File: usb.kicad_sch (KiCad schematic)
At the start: 9 parts, among them J4 CONN_02X03, U1 LFE5U-85F-6BG381C, U6 FT231XS, Y1 ECS-1612MV-250-CN-TR

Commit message: in progress, placement happend -- working on wiring
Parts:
- J4: footprint Socket_Strips:Socket_Strip_Straight_2x03 -> Connector_PinSocket_2.54mm:PinSocket_2x03_P2.54mm_Vertical

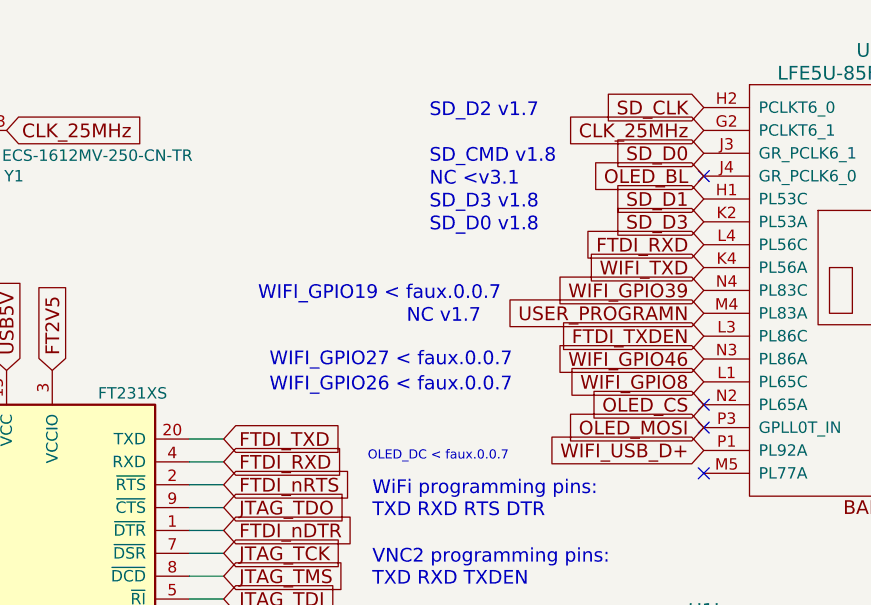
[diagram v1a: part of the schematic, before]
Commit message: done with routing
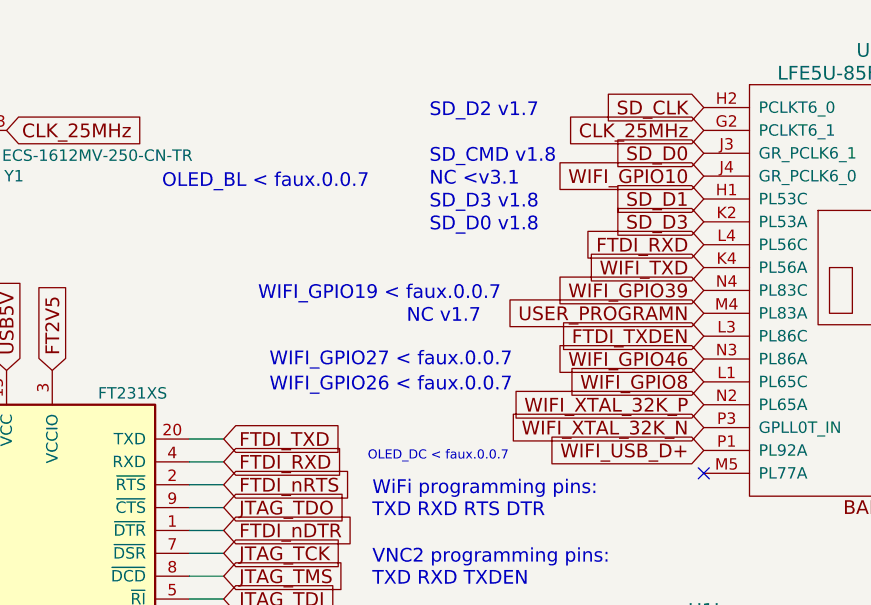
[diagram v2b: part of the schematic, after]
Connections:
- net OLED_BL renamed WIFI_GPIO10
- net OLED_CS renamed WIFI_XTAL_32K_P
- net OLED_MOSI renamed WIFI_XTAL_32K_N
- no-connect marks 8 -> 5
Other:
- note added: "OLED_BL < faux.0.0.7"
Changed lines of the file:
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@@
+		)
+	)
+	(text "OLED_BL < faux.0.0.7"
+		(exclude_from_sim no)
+		(at 159.512 43.434 0)
+		(effects
+			(font
+				(size 1.524 1.524)
+			)
+			(justify left bottom)
 		)
 	)
@@
 	)
 	(no_connect
-		(at 219.71 69.85)
-	)
-	(no_connect
-		(at 219.71 67.31)
-	)
-	(no_connect
 		(at 46.99 50.8)
 	)
@@
 		(at 219.71 74.93)
 	)
-	(no_connect
-		(at 219.71 41.91)
-	)
 	(wire
 		(pts
@@
 		)
 	)
-	(global_label "OLED_BL"
+	(global_label "WIFI_GPIO10"
 		(shape input)
 		(at 219.71 41.91 180)
@@
 		)
 	)
-	(global_label "OLED_MOSI"
+	(global_label "WIFI_XTAL_32K_N"
 		(shape input)
 		(at 219.71 69.85 180)
@@
 		)
 	)
-	(global_label "OLED_CS"
+	(global_label "WIFI_XTAL_32K_P"
 		(shape input)
 		(at 219.71 67.31 180)

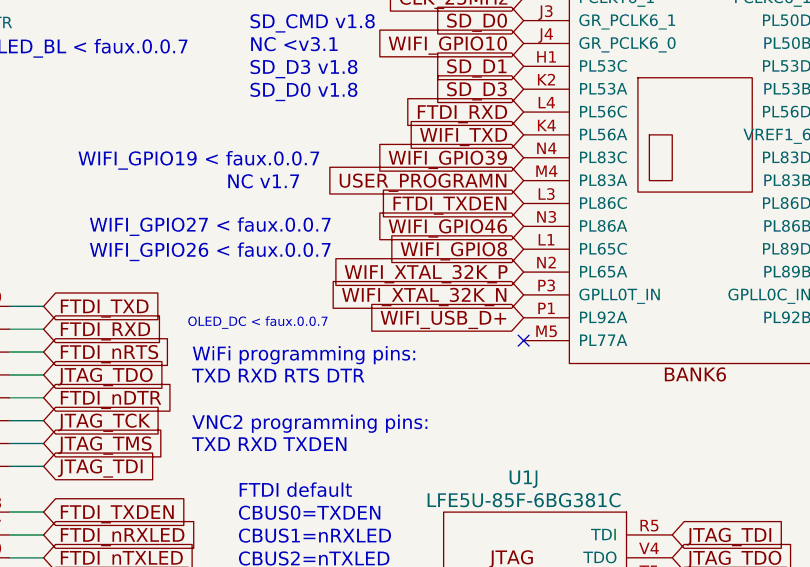
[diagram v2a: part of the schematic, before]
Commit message: fix diff pairs
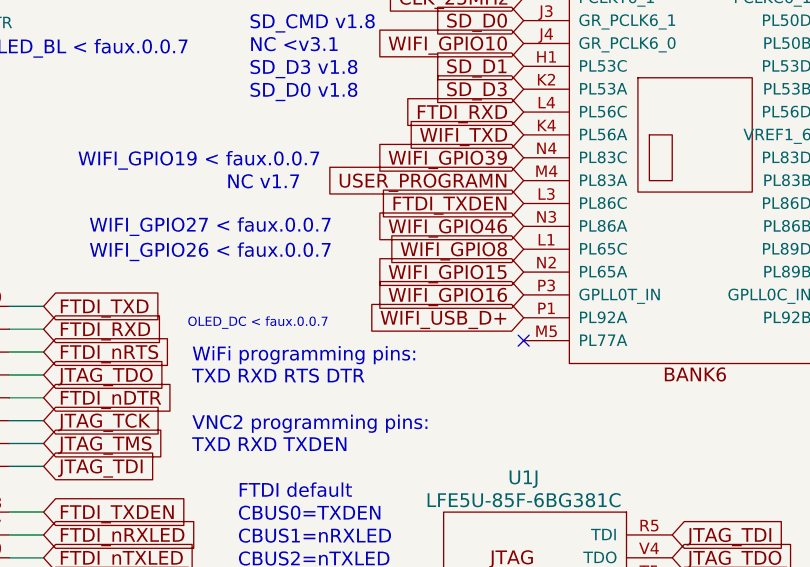
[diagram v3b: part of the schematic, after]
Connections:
- net WIFI_XTAL_32K_N renamed WIFI_GPIO16
- net WIFI_XTAL_32K_P renamed WIFI_GPIO15
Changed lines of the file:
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@@
 		)
 	)
-	(global_label "WIFI_XTAL_32K_N"
+	(global_label "WIFI_GPIO16"
 		(shape input)
 		(at 219.71 69.85 180)
@@
 		)
 	)
-	(global_label "WIFI_XTAL_32K_P"
+	(global_label "WIFI_GPIO15"
 		(shape input)
 		(at 219.71 67.31 180)

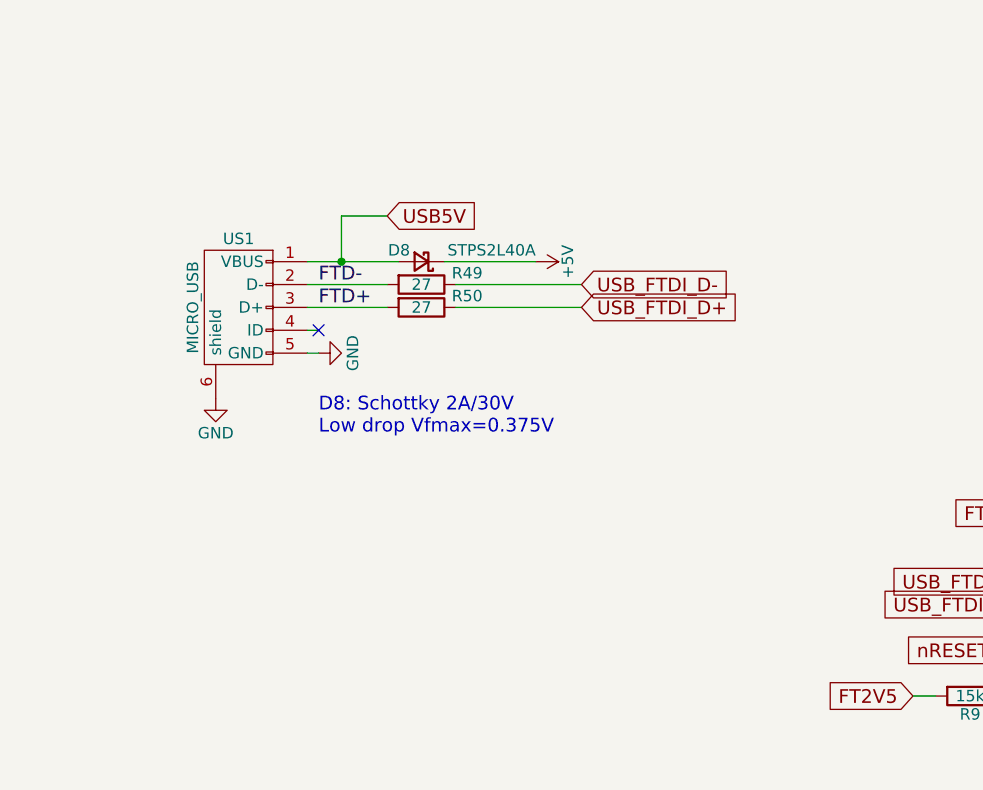
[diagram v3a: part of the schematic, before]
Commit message: switch to usb-c. upgrade to v1.0.4
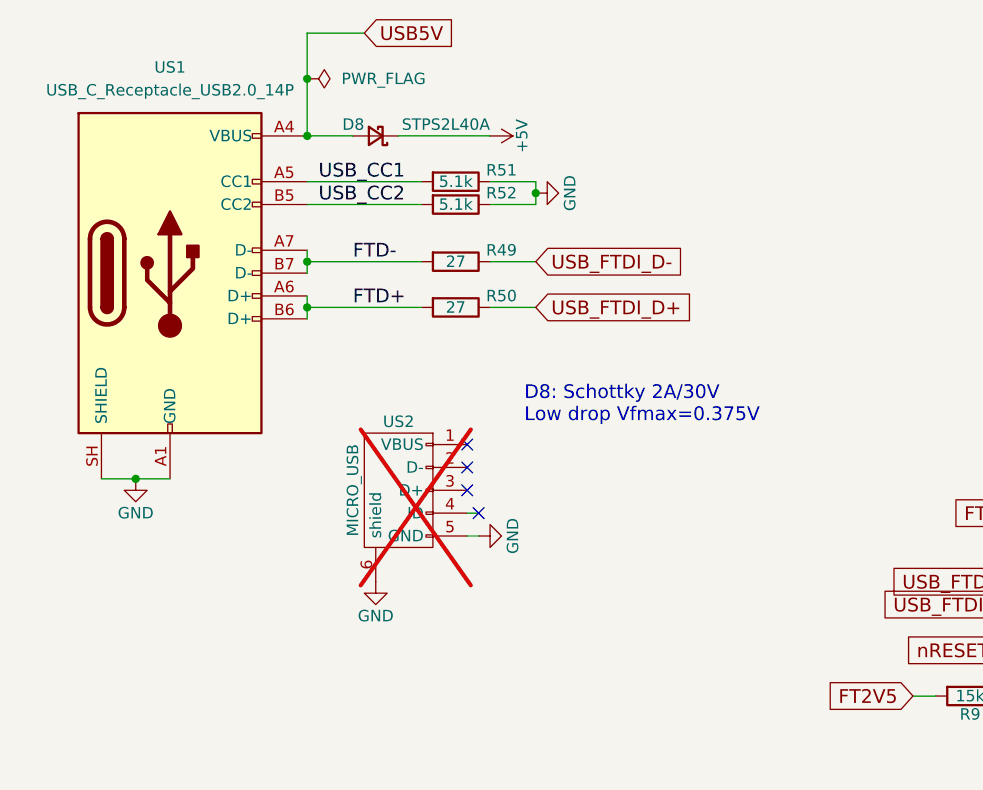
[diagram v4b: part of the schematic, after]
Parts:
- added R51, R52: 5.1k, Resistor_SMD:R_0603_1608Metric, symbol Device:R
- added US1: USB_C_Receptacle_USB2.0_14P, Connector_USB:USB_C_Receptacle_GCT_USB4085, symbol Connector:USB_C_Receptacle_USB2.0_14P
- US2: renamed from US1; now not fitted; now left out of the parts list
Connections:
- net FTD+: now also US1.A6 (D+), US1.B6 (D+); no longer US2.3 (D+)
- net FTD-: now also US1.A7 (D-), US1.B7 (D-); no longer US2.2 (D-)
- net GND: now also R51.1, R52.1, US1.A1 (GND), US1.A12 (GND), US1.B1 (GND), US1.B12 (GND), US1.SH (SHIELD)
- net USB5V: now also US1.A4 (VBUS), US1.A9 (VBUS), US1.B4 (VBUS), US1.B9 (VBUS); no longer US2.1 (VBUS)
- new net USB_CC1: R51.2, US1.A5 (CC1)
- new net USB_CC2: R52.2, US1.B5 (CC2)
- no-connect marks 5 -> 8
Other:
- moved on the sheet: D8, R49, R50

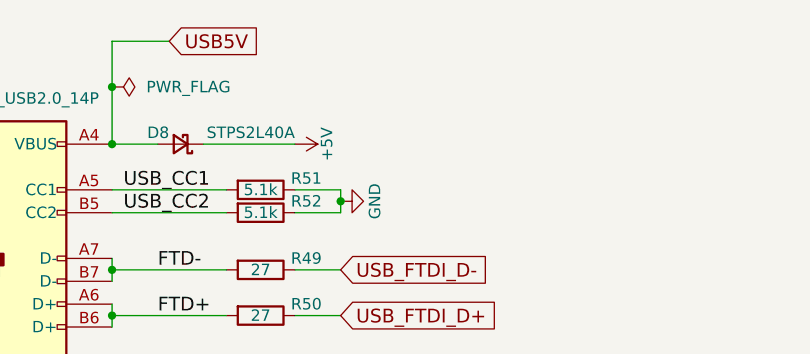
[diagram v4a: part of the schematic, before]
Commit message: add fids, add attributions on board, bump to v1.0.5
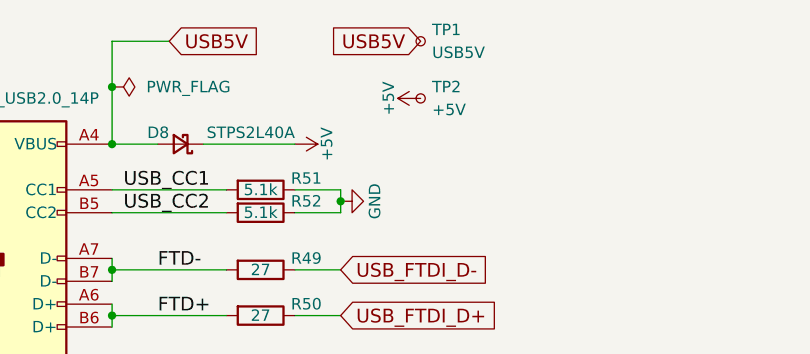
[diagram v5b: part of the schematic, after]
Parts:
- added TP1: USB5V, TestPoint:TestPoint_Pad_D1.0mm, symbol Connector:TestPoint_Small
- added TP2: +5V, TestPoint:TestPoint_Pad_D1.0mm, symbol Connector:TestPoint_Small
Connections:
- net +5V: now also TP2.1
- net USB5V: now also TP1.1

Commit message: this should have gone with the prev. commit
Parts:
- TP1, TP2: now left out of the parts list
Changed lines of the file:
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@@
 		(body_style 1)
 		(exclude_from_sim no)
-		(in_bom yes)
+		(in_bom no)
 		(on_board yes)
 		(in_pos_files yes)
@@
 		(body_style 1)
 		(exclude_from_sim no)
-		(in_bom yes)
+		(in_bom no)
 		(on_board yes)
 		(in_pos_files yes)
@@
 		(body_style 1)
 		(exclude_from_sim no)
-		(in_bom yes)
+		(in_bom no)
 		(on_board yes)
 		(in_pos_files yes)

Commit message: make MPN reflect mouser part numbers
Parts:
- R49, R50: MPN AC0603JR-0727RL -> 603-AC0603JR-0727RL
- R9: MPN RC0603FR-0715KL -> 603-RC0603FR-0715KL
- U1: MPN LFE5U-85F-6BG381C -> 842-LFE5U85F6BG381C
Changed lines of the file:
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@@
 			)
 		)
-		(property "MPN" "RC0603FR-0715KL"
+		(property "MPN" "603-RC0603FR-0715KL"
 			(at 119.38 91.44 90)
 			(hide yes)
@@
 			)
 		)
-		(property "MPN" "AC0603JR-0727RL"
+		(property "MPN" "603-AC0603JR-0727RL"
 			(at 62.23 43.18 90)
 			(hide yes)
@@
 			)
 		)
-		(property "MPN" "AC0603JR-0727RL"
+		(property "MPN" "603-AC0603JR-0727RL"
 			(at 62.23 48.26 90)
 			(hide yes)
@@
 			)
 		)
-		(property "MPN" "LFE5U-85F-6BG381C"
+		(property "MPN" "842-LFE5U85F6BG381C"
 			(at 238.76 52.07 0)
 			(hide yes)
@@
 			)
 		)
-		(property "MPN" "LFE5U-85F-6BG381C"
+		(property "MPN" "842-LFE5U85F6BG381C"
 			(at 218.44 100.33 0)
 			(hide yes)

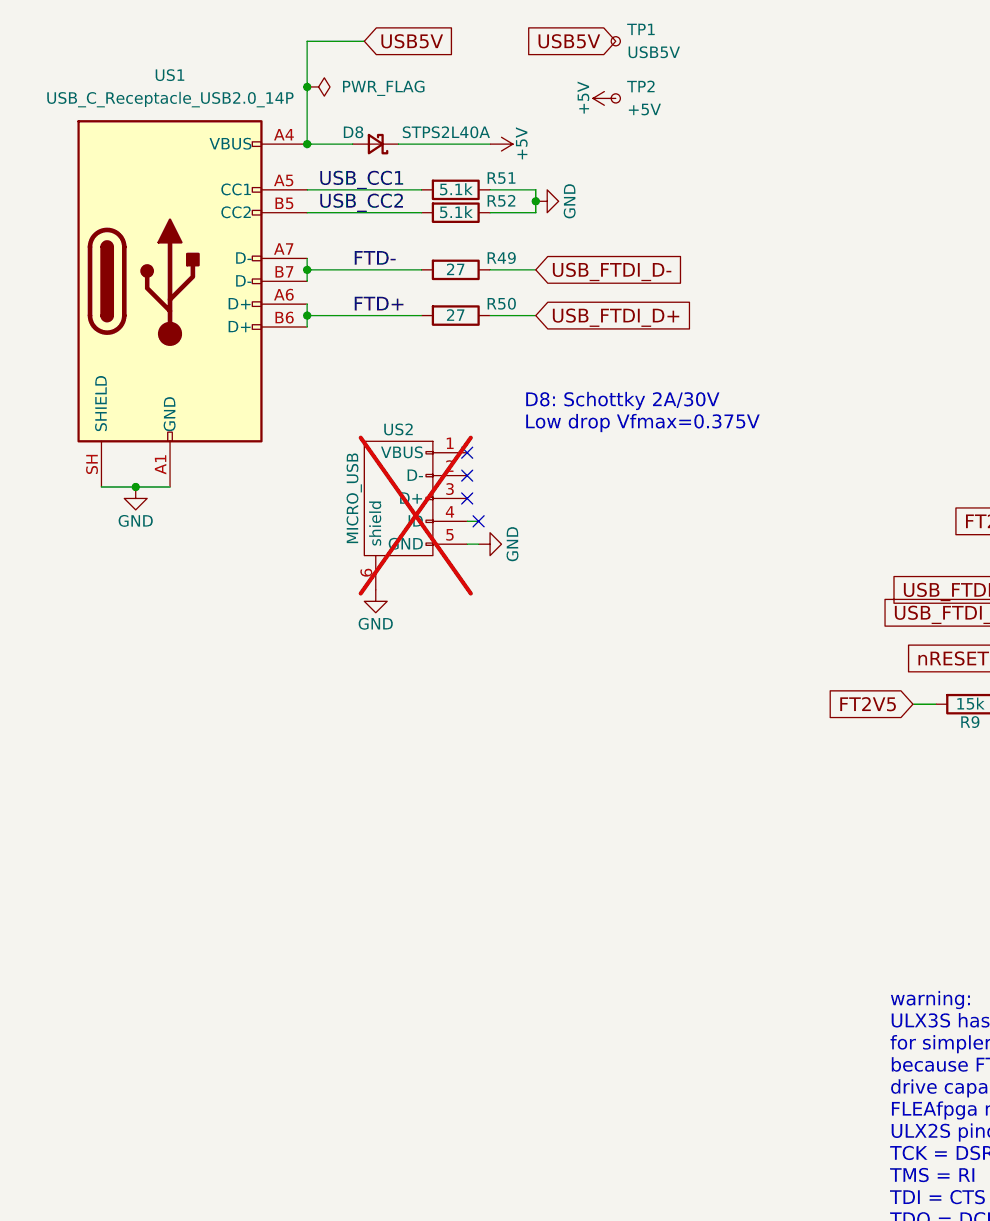
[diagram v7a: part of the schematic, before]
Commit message: add secondary power-only usb-c connector. v1.0.9
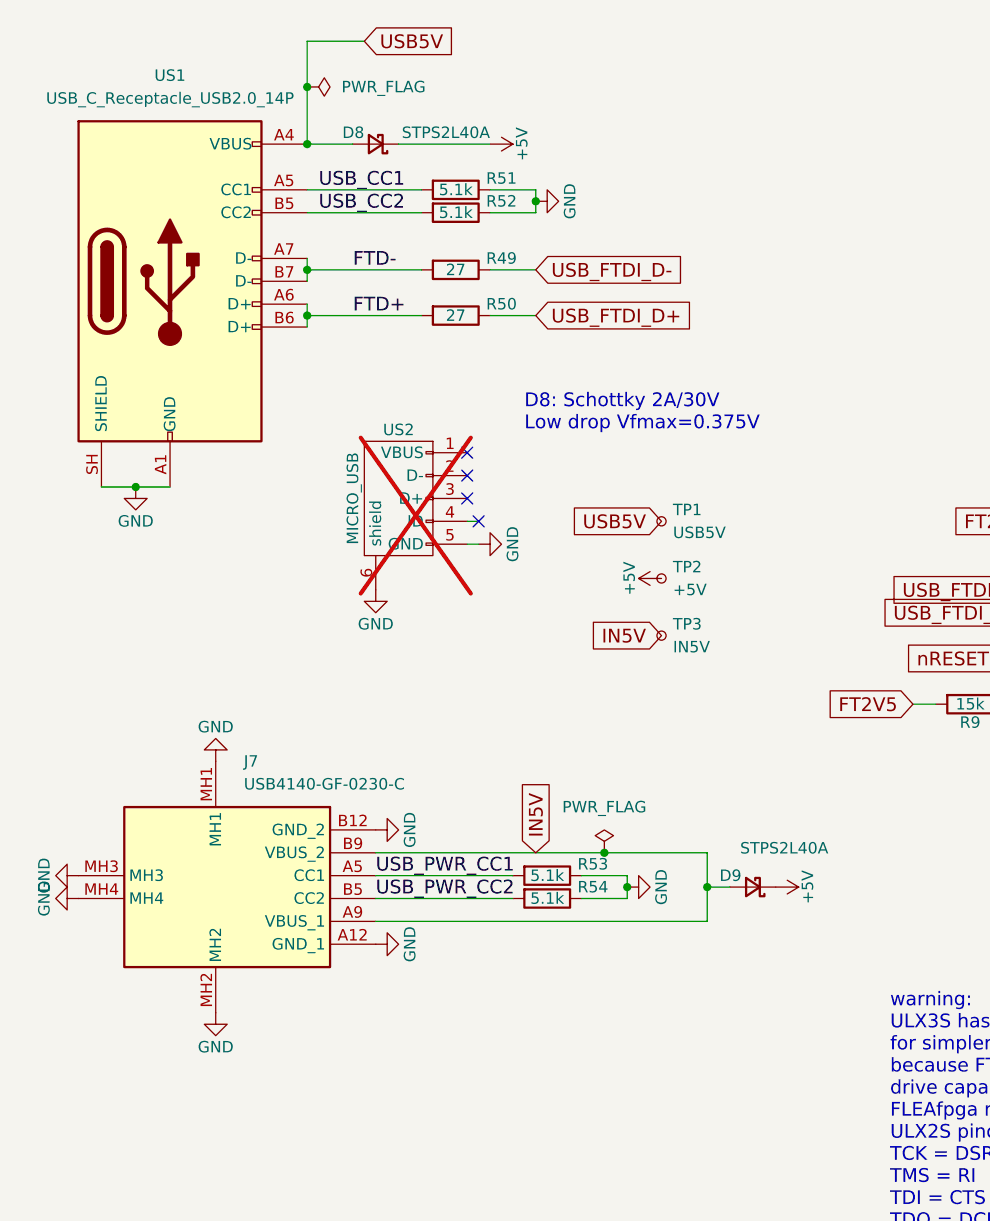
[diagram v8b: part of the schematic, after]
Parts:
- added D9: STPS2L40A, Diode_SMD:D_SMA, symbol Device:D_Schottky_Small
- added J7: USB4140-GF-0230-C, usb_c:USB4140GF0230C, symbol usb-c-0230:USB4140-GF-0230-C
- added R53, R54: 5.1k, Resistor_SMD:R_0603_1608Metric, symbol Device:R
- added TP3: IN5V, TestPoint:TestPoint_Pad_D1.0mm, symbol Connector:TestPoint_Small
- J4: footprint Connector_PinSocket_2.54mm:PinSocket_2x03_P2.54mm_Vertical -> Connector_PinSocket_2.54mm:PinSocket_2x03_P2.54mm_Vertical_SMD
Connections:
- net +5V: now also D9.1 (K)
- net GND: now also J7.A12 (GND_1), J7.B12 (GND_2), J7.MH1, J7.MH2, J7.MH3, J7.MH4, R53.1, R54.1
- new net IN5V: D9.2 (A), J7.A9 (VBUS_1), J7.B9 (VBUS_2), TP3.1
- new net USB_PWR_CC1: J7.A5 (CC1), R53.2
- new net USB_PWR_CC2: J7.B5 (CC2), R54.2
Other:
- moved on the sheet: TP1, TP2
